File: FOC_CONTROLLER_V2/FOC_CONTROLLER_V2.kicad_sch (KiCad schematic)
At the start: 87 parts, among them IC1 STSPIN32G4, J1 DC IN, J2 Conn_01x01, J3 Conn_01x01, J4 Conn_01x01, J5 ENCODER, J6 JTAG, SW3 SW_DIP_x02, U1 THVD1520, U2 THVD1520

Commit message: Routage Phases PCB
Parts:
- removed C19, C20: 4u7, Capacitor_SMD:C_1210_3225Metric, symbol Device:C_Small
- removed C21: 1u, Capacitor_SMD:C_0603_1608Metric, symbol Device:C_Small
- removed C22: 47u, Capacitor_SMD:C_0603_1608Metric, symbol Device:C_Small
- removed PS1: 171013801, SamacSys_Parts:171013801, symbol SamacSys_Parts:171013801
- removed R31: 5k6, Resistor_SMD:R_0402_1005Metric, symbol Device:R
- removed R32: 402k, Resistor_SMD:R_0402_1005Metric, symbol Device:R
- removed R33: 80k6, Resistor_SMD:R_0402_1005Metric, symbol Device:R
- removed U1: THVD1520, Package_SO:SOIC-8_3.9x4.9mm_P1.27mm, symbol Custom_symbol:THVD1520
- added C13: 10u, Capacitor_SMD:C_0603_1608Metric, symbol Device:C_Small
- added C16: N.M., Capacitor_SMD:C_0603_1608Metric, symbol Device:C_Small
- added C19: 10u, Capacitor_SMD:C_0805_2012Metric_Pad1.18x1.45mm_HandSolder, symbol Device:C
- added C20: 22u, Capacitor_SMD:C_0805_2012Metric_Pad1.18x1.45mm_HandSolder, symbol Device:C
- added C28, C29: 100n, Capacitor_SMD:C_0603_1608Metric, symbol Device:C_Small
- added C30: 220n, Capacitor_SMD:C_0603_1608Metric, symbol Device:C_Small
- added D4: STPS0560Z, Diode_SMD:D_SOD-123, symbol Device:D_Zener
- added J10: R-78B5.0-2.0, Package_TO_SOT_SMD:SOT-223, symbol Regulator_Switching:R-78B5.0-2.0
- added J7, J8: Conn_SW_2, Connector_JST:JST_GH_SM02B-GHS-TB_1x02-1MP_P1.25mm_Horizontal, symbol Connector_Generic:Conn_01x02
- added J9: USB_C_Receptacle_USB2.0_14P, Connector_USB:USB_C_Receptacle_G-Switch_GT-USB-7010ASV, symbol Connector:USB_C_Receptacle_USB2.0_14P
- added JP1: SolderJumper_3_Open, Jumper:SolderJumper-3_P1.3mm_Open_RoundedPad1.0x1.5mm_NumberLabels, symbol Jumper:SolderJumper_3_Open
- added L1: 15u, Footprint:L_Wurth_WE-MXGI-5030, symbol Device:L_Small
- added R49, R51: 100k, Capacitor_SMD:C_0603_1608Metric, symbol Device:R_Small
- added R50, R52: 200, Capacitor_SMD:C_0603_1608Metric, symbol Device:R_Small
- added R53: 10, Resistor_SMD:R_0603_1608Metric, symbol Device:R_Small
- C17: footprint Capacitor_SMD:C_0201_0603Metric -> Capacitor_SMD:C_0603_1608Metric
- J2, J3, J4: footprint Footprint:REDCUBE SMT -> Footprint:REDCUBETHT_74651173R
- J5: footprint Connector_JST:JST_SH_SM04B-SRSS-TB_1x04-1MP_P1.00mm_Horizontal -> Connector_JST:JST_GH_SM04B-GHS-TB_1x04-1MP_P1.25mm_Horizontal
- U1: renamed from U2; value THVD1520 -> THVD1400
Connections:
- net +24V: no longer C2.1, J1.1 (Pin_1), R28.1
- net +3.3V: now also J7.1 (Pin_1), J8.1 (Pin_1), JP1.1 (A)
- net +48V: now also C2.1, J1.1 (Pin_1), R28.1; no longer IC1.62 (SW)
- net +5V: now also C19.1, J10.1 (IN), J9.A4 (VBUS), J9.A9 (VBUS), J9.B4 (VBUS), J9.B9 (VBUS); no longer IC1.63 (VCC), IC1.64 (REGIN)
- net A: now also J9.A6 (D+), J9.B6 (D+), R53.1
- net B: now also J9.A7 (D-), J9.B7 (D-), R53.2
- net DRIVE_EN: now also U1.2 (~{RE})
- net GND: now also U1.5 (GND), C13.2, C16.2, C19.2, C20.2, C28.1, C29.1, C30.2, D4.2 (A), J10.2 (GND), J9.A1 (GND), J9.A12 (GND), J9.B1 (GND), J9.B12 (GND), J9.S1 (SHIELD), R49.2, R51.2
- net OPN1: now also IC1.25 (PB2); no longer IC1.16 (PA3)
- net OPN3: now also IC1.16 (PA3); no longer IC1.25 (PB2)
- net OPO1: now also IC1.24 (PB1); no longer IC1.15 (PA2)
- net OPO3: now also IC1.15 (PA2); no longer IC1.24 (PB1)
- net OPP1: now also IC1.23 (PB0); no longer IC1.14 (PA1)
- net OPP3: now also IC1.14 (PA1); no longer IC1.23 (PB0)
- net RECIEVE_EN: now also U1.3 (DE)
- net UART_RX: now also U1.4 (D)
- net UART_TX: now also U1.1 (R)
- net at U1.6 (A): now also R37.1
- net at U1.7 (B): now also R36.1
- net at U1.8 (VCC): now also C30.1, JP1.2 (C)
- net L_SW_2: now reaches IC1.59 (PB8)
- net L_SW_2: now also R52.2
- net L_SW_1: now reaches IC1.60 (PB9)
- net L_SW_1: now also R50.2
- new net: C13.1, C16.1, IC1.63 (VCC), IC1.64 (REGIN), L1.2
- new net +3,3V_EXT: C20.1, J10.3 (OUT), JP1.3 (B)
- new net Conn_SW_1: C28.2, J7.2 (Pin_2), R49.1, R50.1
- new net Conn_SW_2: C29.2, J8.2 (Pin_2), R51.1, R52.1
- new net SW: D4.1 (K), IC1.62 (SW), L1.1
- no-connect marks 12 -> 13
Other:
- note added: "LDO"
- note removed: "Buck 24V->5V"
- note removed: "RS_485 tranciever on 3.3V"
- moved on the sheet: C18, C8, C9, D2, H1, H2, H3, H4, R12, R30, R34, R35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

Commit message: Routage PCB 99%
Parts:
- added TP19: 24V, TestPoint:TestPoint_Pad_D1.0mm, symbol Connector:TestPoint
- C2: footprint Capacitor_SMD:CP_Elec_10x10.5 -> Capacitor_SMD:CP_Elec_18x22
- J10: value R-78B5.0-2.0 -> AZ1117
- renumbered TP19 to TP20, TP20 to TP21, TP21 to TP22
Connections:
- net +24V: no longer D5.2 (A)
- net +48V: now also D5.2 (A)
- net DRIVE_EN: now also IC1.48 (PA12); no longer IC1.47 (PA11)
- net PB6: now also TP19.1
- net RECIEVE_EN: now also IC1.47 (PA11); no longer IC1.48 (PA12)
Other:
- moved on the sheet: TP20, TP21, TP22
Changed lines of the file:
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@@
 	(wire
 		(pts
+			(xy 124.46 238.76) (xy 139.7 238.76)
+		)
+		(stroke
+			(width 0)
+			(type default)
+		)
+	)
+	(wire
+		(pts
 			(xy 78.74 175.26) (xy 82.55 175.26)
 		)
@@
 	(wire
 		(pts
-			(xy 137.16 242.57) (xy 124.46 242.57)
+			(xy 137.16 246.38) (xy 124.46 246.38)
 		)
 		(stroke
@@
 	(wire
 		(pts
-			(xy 137.16 238.76) (xy 124.46 238.76)
+			(xy 137.16 242.57) (xy 124.46 242.57)
 		)
 		(stroke
@@
 	(wire
 		(pts
-			(xy 124.46 246.38) (xy 137.16 246.38)
+			(xy 124.46 250.19) (xy 137.16 250.19)
 		)
 		(stroke
@@
 	)
 	(label "DRIVE_EN"
-		(at 144.78 68.58 180)
+		(at 144.78 66.04 180)
 		(effects
 			(font
@@
 		)
 	)
+	(label "PB6"
+		(at 139.7 238.76 180)
+		(effects
+			(font
+				(size 1.27 1.27)
+			)
+			(justify right bottom)
+		)
+	)
 	(label "GLS2"
 		(at 114.3 130.81 90)
@@
 	)
 	(label "RECIEVE_EN"
-		(at 144.78 66.04 180)
+		(at 144.78 68.58 180)
 		(effects
 			(font
@@
 			)
 		)
-		(property "Value" "+24V"
+		(property "Value" "+48V"
 			(at 238.76 85.09 0)
 			(effects
@@
 	(symbol
 		(lib_id "Connector:TestPoint")
-		(at 124.46 238.76 90)
+		(at 124.46 242.57 90)
 		(unit 1)
 		(exclude_from_sim no)
@@
 		(on_board yes)
 		(dnp no)
-		(property "Reference" "TP19"
-			(at 117.602 238.76 90)
+		(property "Reference" "TP20"
+			(at 117.602 242.57 90)
 			(effects
 				(font
@@
 		)
 		(property "Value" "24V"
-			(at 122.682 243.332 0)
+			(at 122.682 247.142 0)
 			(effects
 				(font
@@
 		)
 		(property "Footprint" "TestPoint:TestPoint_Pad_D1.0mm"
-			(at 124.46 233.68 0)
+			(at 124.46 237.49 0)
 			(effects
 				(font
@@
 		)
 		(property "Datasheet" "~"
-			(at 124.46 233.68 0)
+			(at 124.46 237.49 0)
 			(effects
 				(font
@@
 		)
 		(property "Description" "test point"
-			(at 124.46 238.76 0)
+			(at 124.46 242.57 0)
 			(effects
 				(font
@@
 			(project "FOC_CONTROLLER_V2"
 				(path "/a5bd1c77-2ac7-4621-b0cb-d4fae8c0736d"
-					(reference "TP19")
+					(reference "TP20")
 					(unit 1)
 				)
@@
 	(symbol
 		(lib_id "Connector:TestPoint")
-		(at 124.46 246.38 90)
+		(at 124.46 250.19 90)
 		(unit 1)
 		(exclude_from_sim no)
@@
 		(on_board yes)
 		(dnp no)
-		(property "Reference" "TP21"
-			(at 117.856 246.38 90)
+		(property "Reference" "TP22"
+			(at 117.856 250.19 90)
 			(effects
 				(font
@@
 		)
 		(property "Value" "3V3"
-			(at 122.682 250.952 0)
+			(at 122.682 254.762 0)
 			(effects
 				(font
@@
 		)
 		(property "Footprint" "TestPoint:TestPoint_Pad_D1.0mm"
-			(at 124.46 241.3 0)
+			(at 124.46 245.11 0)
 			(effects
 				(font
@@
 		)
 		(property "Datasheet" "~"
-			(at 124.46 241.3 0)
+			(at 124.46 245.11 0)
 			(effects
 				(font
@@
 		)
 		(property "Description" "test point"
-			(at 124.46 246.38 0)
+			(at 124.46 250.19 0)
 			(effects
 				(font
@@
 			(project "FOC_CONTROLLER_V2"
 				(path "/a5bd1c77-2ac7-4621-b0cb-d4fae8c0736d"
-					(reference "TP21")
+					(reference "TP22")
 					(unit 1)
 				)
@@
 	(symbol
 		(lib_id "power:+24V")
-		(at 137.16 238.76 270)
+		(at 137.16 242.57 270)
 		(unit 1)
 		(exclude_from_sim no)
@@
 		(dnp no)
 		(property "Reference" "#PWR053"
-			(at 133.35 238.76 0)
+			(at 133.35 242.57 0)
 			(effects
 				(font
@@
 		)
 		(property "Value" "+24V"
-			(at 135.636 237.49 90)
+			(at 135.636 241.3 90)
 			(effects
 				(font
@@
 		)
 		(property "Footprint" ""
-			(at 137.16 238.76 0)
+			(at 137.16 242.57 0)
 			(effects
 				(font
@@
 		)
 		(property "Datasheet" ""
-			(at 137.16 238.76 0)
+			(at 137.16 242.57 0)
 			(effects
 				(font
@@
 		)
 		(property "Description" "Power symbol creates a global label with name \"+24V\""
-			(at 137.16 238.76 0)
+			(at 137.16 242.57 0)
 			(effects
 				(font
@@
 	(symbol
 		(lib_id "power:+3.3V")
-		(at 137.16 246.38 270)
+		(at 137.16 250.19 270)
 		(unit 1)
 		(exclude_from_sim no)
@@
 		(dnp no)
 		(property "Reference" "#PWR055"
-			(at 133.35 246.38 0)
+			(at 133.35 250.19 0)
 			(effects
 				(font
@@
 		)
 		(property "Value" "+3.3V"
-			(at 132.588 245.11 90)
+			(at 132.588 248.92 90)
 			(effects
 				(font
@@
 		)
 		(property "Footprint" ""
-			(at 137.16 246.38 0)
+			(at 137.16 250.19 0)
 			(effects
 				(font
@@
 		)
 		(property "Datasheet" ""
-			(at 137.16 246.38 0)
+			(at 137.16 250.19 0)
 			(effects
 				(font
@@
 		)
 		(property "Description" "Power symbol creates a global label with name \"+3.3V\""
-			(at 137.16 246.38 0)
+			(at 137.16 250.19 0)
 			(effects
 				(font
@@
 			)
 		)
-		(property "Footprint" "Capacitor_SMD:CP_Elec_10x10.5"
+		(property "Footprint" "Capacitor_SMD:CP_Elec_18x22"
 			(at 36.83 162.56 0)
 			(effects
@@
 	(symbol
 		(lib_id "power:+5V")
-		(at 137.16 242.57 270)
+		(at 137.16 246.38 270)
 		(unit 1)
 		(exclude_from_sim no)
@@
 		(dnp no)
 		(property "Reference" "#PWR054"
-			(at 133.35 242.57 0)
+			(at 133.35 246.38 0)
 			(effects
 				(font
@@
 		)
 		(property "Value" "+5V"
-			(at 134.112 241.3 90)
+			(at 134.112 245.11 90)
 			(effects
 				(font
@@
 		)
 		(property "Footprint" ""
-			(at 137.16 242.57 0)
+			(at 137.16 246.38 0)
 			(effects
 				(font
@@
 		)
 		(property "Datasheet" ""
-			(at 137.16 242.57 0)
+			(at 137.16 246.38 0)
 			(effects
 				(font
@@
 		)
 		(property "Description" "Power symbol creates a global label with name \"+5V\""
-			(at 137.16 242.57 0)
+			(at 137.16 246.38 0)
 			(effects
 				(font
@@
 	)
 	(symbol
+		(lib_id "Connector:TestPoint")
+		(at 124.46 238.76 90)
+		(unit 1)
+		(exclude_from_sim no)
+		(in_bom yes)
+		(on_board yes)
+		(dnp no)
+		(property "Reference" "TP19"
+			(at 117.602 238.76 90)
+			(effects
+				(font
+					(size 1.27 1.27)
+				)
+			)
+		)
+		(property "Value" "24V"
+			(at 122.682 243.332 0)
+			(effects
+				(font
+					(size 1.27 1.27)
+				)
+				(hide yes)
+			)
+		)
+		(property "Footprint" "TestPoint:TestPoint_Pad_D1.0mm"
+			(at 124.46 233.68 0)
+			(effects
+				(font
+					(size 1.27 1.27)
+				)
+				(hide yes)
+			)
+		)
+		(property "Datasheet" "~"
+			(at 124.46 233.68 0)
+			(effects
+				(font
+					(size 1.27 1.27)
+				)
+				(hide yes)
+			)
+		)
+		(property "Description" "test point"
+			(at 124.46 238.76 0)
+			(effects
+				(font
+					(size 1.27 1.27)
+				)
+				(hide yes)
+			)
+		)
+		(pin "1"
+		)
+		(instances
+			(project "FOC_CONTROLLER_V2"
+				(path "/a5bd1c77-2ac7-4621-b0cb-d4fae8c0736d"
+					(reference "TP19")
+					(unit 1)
+				)
+			)
+		)
+	)
+	(symbol
 		(lib_id "Device:C_Small")
 		(at 53.34 44.45 0)
@@
 			)
 		)
-		(property "Value" "R-78B5.0-2.0"
+		(property "Value" "AZ1117"
 			(at 345.44 158.75 0)
 			(effects
@@
 	(symbol
 		(lib_id "Connector:TestPoint")
-		(at 124.46 242.57 90)
+		(at 124.46 246.38 90)
 		(unit 1)
 		(exclude_from_sim no)
@@
 		(on_board yes)
 		(dnp no)
-		(property "Reference" "TP20"
-			(at 117.856 242.57 90)
+		(property "Reference" "TP21"
+			(at 117.856 246.38 90)
 			(effects
 				(font
@@
 		)
 		(property "Value" "5V"
-			(at 122.682 247.142 0)
+			(at 122.682 250.952 0)
 			(effects
 				(font
@@
 		)
 		(property "Footprint" "TestPoint:TestPoint_Pad_D1.0mm"
-			(at 124.46 237.49 0)
+			(at 124.46 241.3 0)
 			(effects
 				(font
@@
 		)
 		(property "Datasheet" "~"
-			(at 124.46 237.49 0)
+			(at 124.46 241.3 0)
 			(effects
 				(font
@@
 		)
 		(property "Description" "test point"
-			(at 124.46 242.57 0)
+			(at 124.46 246.38 0)
 			(effects
 				(font
@@
 			(project "FOC_CONTROLLER_V2"
 				(path "/a5bd1c77-2ac7-4621-b0cb-d4fae8c0736d"
-					(reference "TP20")
+					(reference "TP21")
 					(unit 1)
 				)

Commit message: PCB driver
Routage terminé
Verifier si l'USB C permet d'avoir un bus et non pas une topologie en étoile
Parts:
- C2: footprint Capacitor_SMD:CP_Elec_18x22 -> Footprint:CP_Wurth_WCAP-ASLL-D16L17
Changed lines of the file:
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@@
 			)
 		)
-		(property "Footprint" "Capacitor_SMD:CP_Elec_18x22"
+		(property "Footprint" "Footprint:CP_Wurth_WCAP-ASLL-D16L17"
 			(at 36.83 162.56 0)
 			(effects

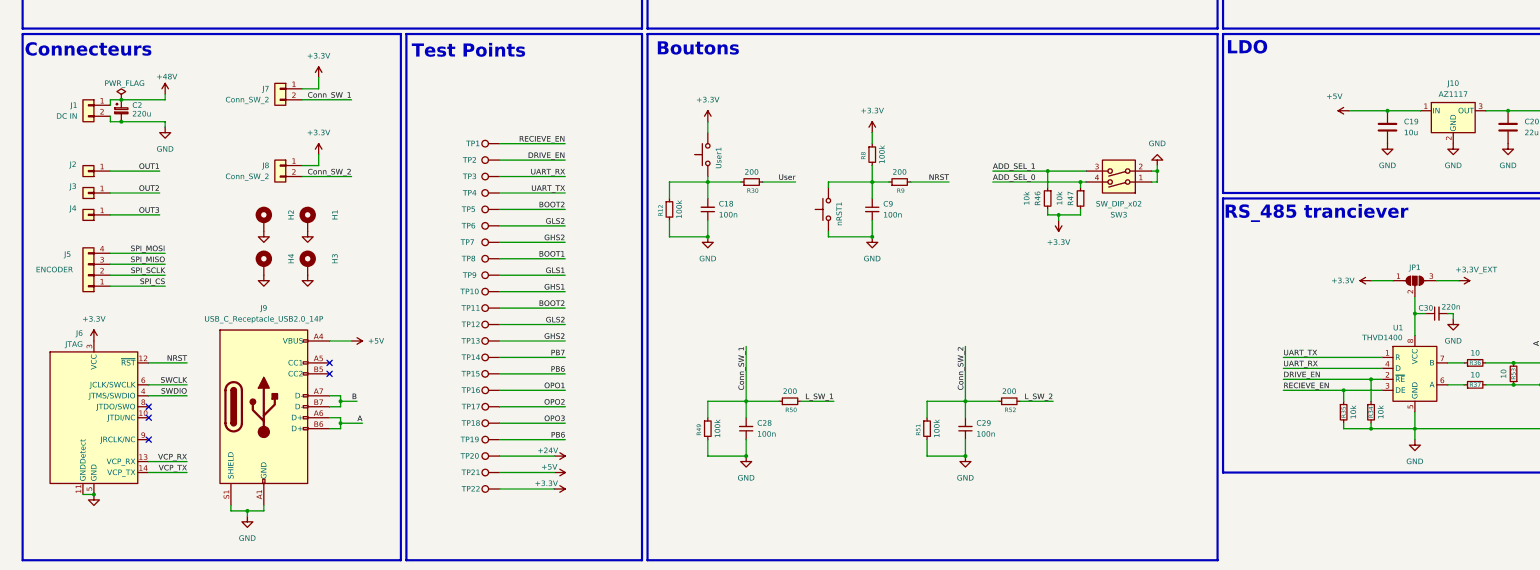
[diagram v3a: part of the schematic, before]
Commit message: PCB driver : DONE
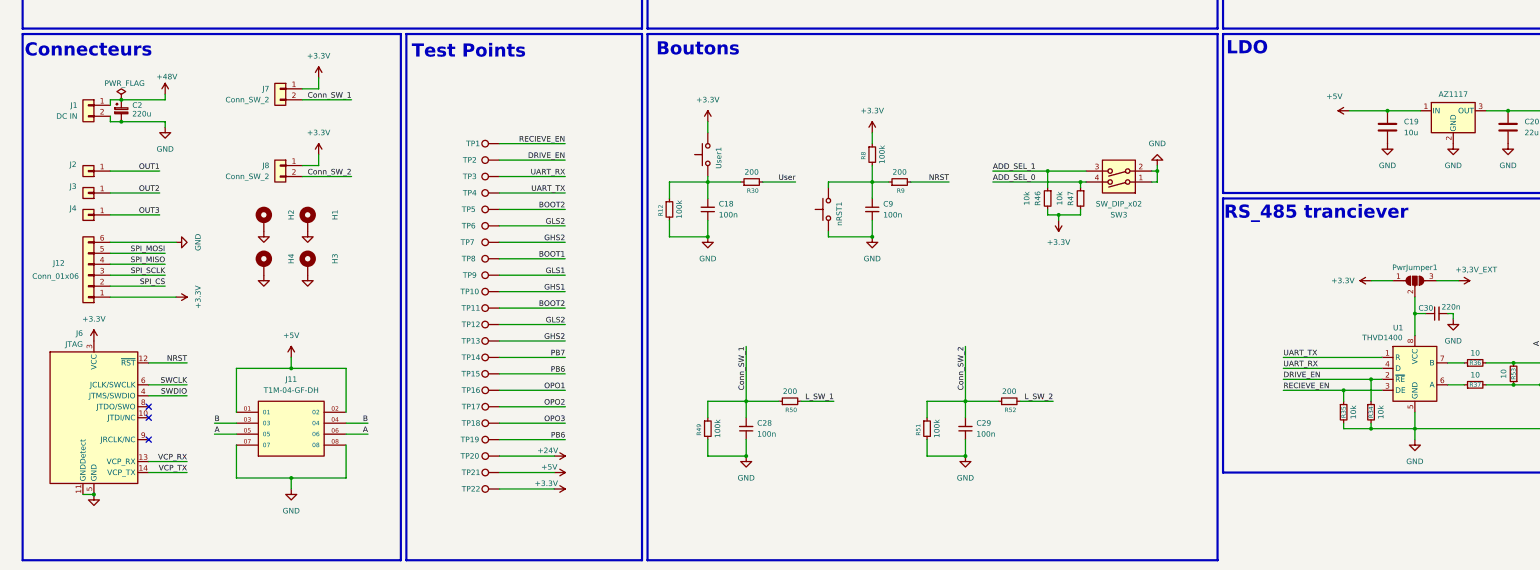
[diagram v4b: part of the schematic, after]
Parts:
- removed J5: ENCODER, Connector_JST:JST_GH_SM04B-GHS-TB_1x04-1MP_P1.25mm_Horizontal, symbol Connector_Generic:Conn_01x04
- removed J9: USB_C_Receptacle_USB2.0_14P, Connector_USB:USB_C_Receptacle_G-Switch_GT-USB-7010ASV, symbol Connector:USB_C_Receptacle_USB2.0_14P
- added J11: T1M-04-GF-DH, Footprint:SAMTEC_T1M-04-GF-DH, symbol T1M:T1M-04-GF-DH
- added J12: Conn_01x06, Connector_JST:JST_GH_SM06B-GHS-TB_1x06-1MP_P1.25mm_Horizontal, symbol Connector_Generic:Conn_01x06
- R30, R49, R50, R51, R52, R8: footprint Capacitor_SMD:C_0603_1608Metric -> Resistor_SMD:R_0603_1608Metric
- renumbered JP1 to PwrJumper1
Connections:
- net +3.3V: now also J12.1 (Pin_1)
- net +5V: now also J11.01, J11.02
- net A: now also J11.05, J11.06
- net B: now also J11.03, J11.04
- net GND: now also J11.07, J11.08, J12.6 (Pin_6)
- net SPI_CS: now also J12.2 (Pin_2)
- net SPI_MISO: now also J12.4 (Pin_4)
- net SPI_MOSI: now also J12.5 (Pin_5)
- net SPI_SCLK: now also J12.3 (Pin_3)
- no-connect marks 13 -> 11
